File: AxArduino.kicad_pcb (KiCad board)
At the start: 2 copper layers, 86 x 33 mm, 35 parts, among them P1 CONN_01X02, P10 CONN_01X04, P11 CONN_01X04, P2 CONN_01X02, P3 CONN_01X03, P4 CONN_01X03, P5 CONN_01X03, P7 CONN_01X03, P8 CONN_01X15, P9 CONN_01X15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

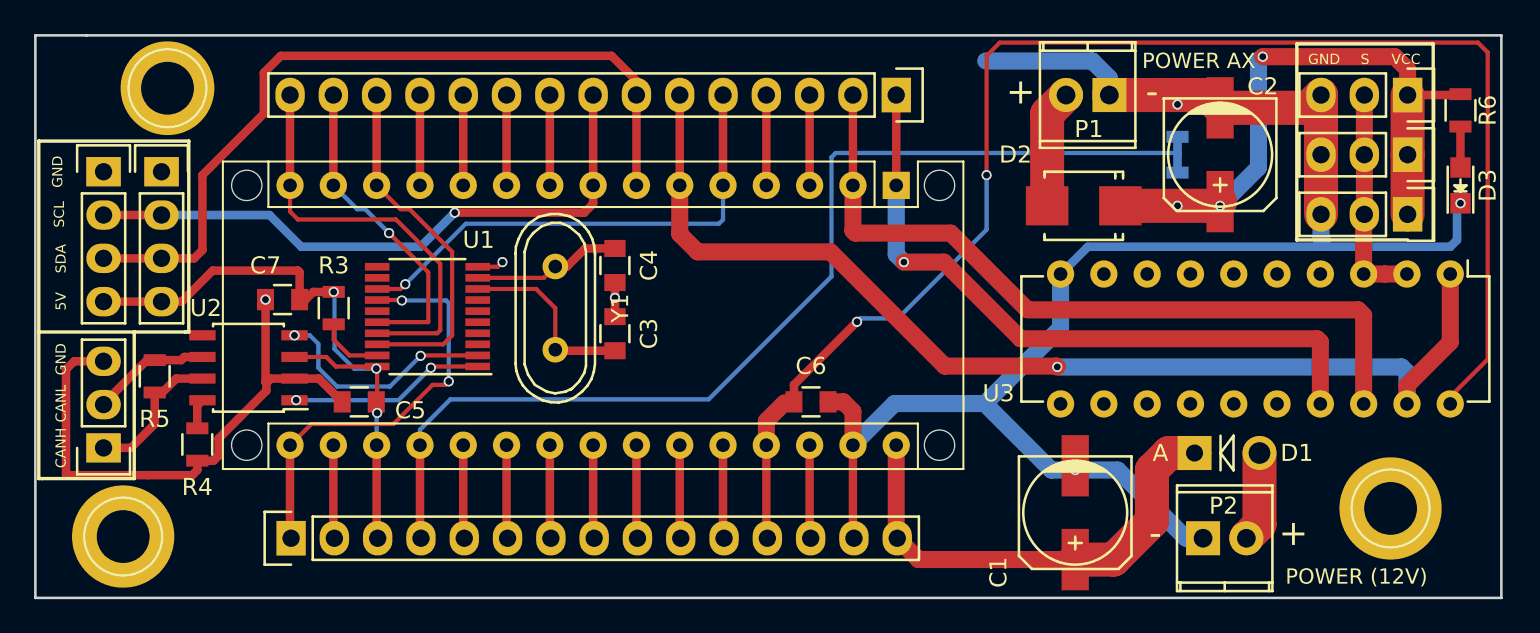
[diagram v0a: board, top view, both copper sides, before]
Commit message: Fixed stuff, like moving r to top layer and adding pullups to i2c
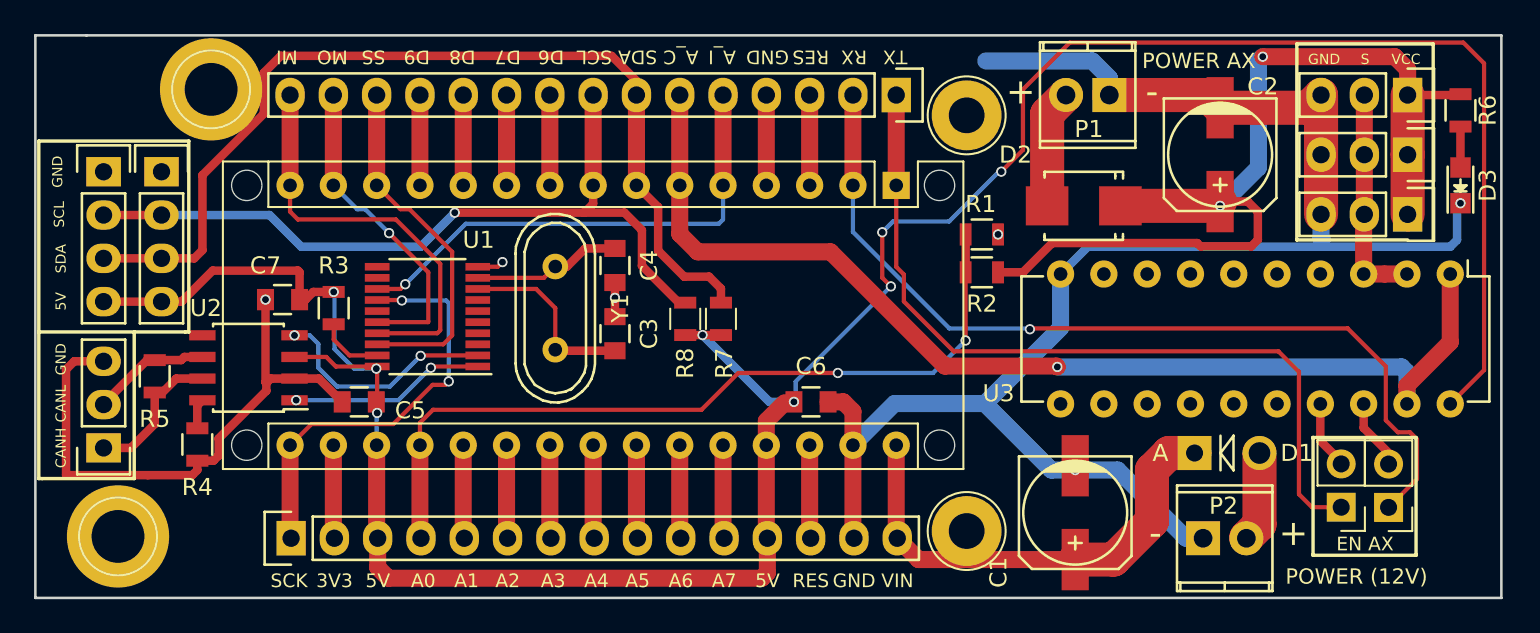
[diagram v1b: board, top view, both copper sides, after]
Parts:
- removed the G*** at (70.0, 87.2)
- removed the REF** at (56.8, 74.1)
- removed the REF** at (54.1, 100.4)
- removed the REF** at (128.5, 98.8)
- added G***: LOGO, Hardware:EP_Logo, B.Cu at (118.2, 77.9)
- added JP1: Jumper, Pin_Headers:Pin_Header_Straight_1x02_Pitch2.54mm, F.Cu at (128.4, 98.7)
- added JP2: Jumper, Pin_Headers:Pin_Header_Straight_1x02_Pitch2.54mm, F.Cu at (125.6, 98.7)
- added R7: 4K7, Resistors_SMD:R_0805, F.Cu at (89.2, 87.6)
- added R8: 4K7, Resistors_SMD:R_0805, F.Cu at (87.1, 87.6)
- added REF**: 1pin, Connectors:1pin, F.Cu at (53.8, 100.4)
- added REF**: 1pin, Connectors:1pin, F.Cu at (59.3, 74.2)
- added REF**: 1pin, Connectors:1pin, F.Cu at (103.6, 75.7)
- added REF**: 1pin, Connectors:1pin, F.Cu at (103.6, 100.1)
- R1, R2: moved to F.Cu
- moved R2 13.3 mm to (104.5, 82.7), turned to 0 degrees
- moved R1 12.5 mm to (104.5, 84.9), turned to 180 degrees
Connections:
- U1 pad 11: (no net) -> Net-(U1-Pad11)
- U1 pad 12: (no net) -> Net-(U1-Pad12)
- U1 pad 15: (no net) -> Net-(U1-Pad15)
- U1 pad 3: (no net) -> Net-(U1-Pad3)
- U1 pad 4: (no net) -> Net-(U1-Pad4)
- U1 pad 5: (no net) -> Net-(U1-Pad5)
- U1 pad 6: (no net) -> Net-(U1-Pad6)
- U1 pad 7: (no net) -> Net-(U1-Pad7)
- U2 pad 5: (no net) -> Net-(U2-Pad5)
- U3 pad 11: (no net) -> Net-(U3-Pad11)
- U3 pad 12: (no net) -> Net-(U3-Pad12)
- U3 pad 13: (no net) -> Net-(U3-Pad13)
- U3 pad 14: (no net) -> Net-(U3-Pad14)
- U3 pad 15: (no net) -> Net-(U3-Pad15)
- U3 pad 16: (no net) -> Net-(U3-Pad16)
- U3 pad 17: A_TX -> A_LS_TX
- U3 pad 18: A_RX -> A_LS_RX
- U3 pad 4: (no net) -> Net-(U3-Pad4)
- U3 pad 5: (no net) -> Net-(U3-Pad5)
- U3 pad 6: (no net) -> Net-(U3-Pad6)
- U3 pad 7: (no net) -> Net-(U3-Pad7)
- U3 pad 8: (no net) -> Net-(U3-Pad8)
- U3 pad 9: (no net) -> Net-(U3-Pad9)
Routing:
- net +5V: track 134.7 -> 164.2 mm, vias 5 -> 8
- net AX_P: track 42.4 -> 62.7 mm, vias 3 -> 2
- net A_A0: track 63.8 -> 47.1 mm, vias 0 -> 2
- net A_SDA: track 46.9 -> 56.7 mm
- net A_SCL: track 36.9 -> 46.3 mm
- net A_RX: track 45.2 -> 52.7 mm, vias 0 -> 1
- net A_TX: track 40.0 -> 47.2 mm, vias 1 -> 0
- net A_LS_RX: track 0.00 -> 4.29 mm
- net A_LS_TX: track 0.00 -> 4.03 mm
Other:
- board text added: "3V3"
- board text added: "A0"
- board text added: "A1"
- board text added: "A2"
- board text added: "A3"
- board text added: "A4"
- board text added: "A5"
- board text added: "A6"
- board text added: "A7"
- board text added: "A_C"
- board text added: "A_I"
- board text added: "D6"
- board text added: "D7"
- board text added: "D8"
- board text added: "D9"
- board text added: "EN AX"
- board text added: "MI"
- board text added: "MO"
- board text added: "RES"
- board text added: "RX"
- board text added: "SCK"
- board text added: "SS"
- board text added: "TX"
- board text added: "VIN"

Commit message: New design
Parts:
- removed C4: C, Capacitors_SMD:C_0805
- removed the G*** at (118.2, 77.9)
- removed P10: CONN_01X04, Pin_Headers:Pin_Header_Straight_1x04
- removed R3: 10K, Resistors_SMD:R_0805
- removed R4: 4.7K, Resistors_SMD:R_0805
- removed R5: 120, Resistors_SMD:R_0805
- removed the REF** at (53.8, 100.4)
- removed the REF** at (59.3, 74.2)
- removed the REF** at (103.6, 75.7)
- removed the REF** at (103.6, 100.1)
- removed U1: MCP2515-I/ST, Housings_SSOP:TSSOP-20_4.4x6.5mm_Pitch0.65mm
- removed U2: MCP2551-I-SN, Housings_SOIC:SOIC-8_3.9x4.9mm_Pitch1.27mm
- removed Y1: Crystal, Crystals:Crystal_HC49-U_Vertical
- added G***: LOGO, Hardware:EP_Logo, B.Cu at (92.7, 103.4)
- added G***: LOGO, Hardware:EP_Logo, F.Cu at (123.4, 111.5)
- added P12: CONN_01X03, Pin_Headers:Pin_Header_Straight_1x03_Pitch2.54mm, F.Cu at (88.5, 110.6)
- added P6: CONN_01X02, Connectors_Terminal_Blocks:TerminalBlock_Pheonix_MKDS1.5-2pol, F.Cu at (95.2, 96.0)
- added REF**: 1pin, Connectors:1pin, F.Cu at (171.7, 122.9)
- added REF**: 1pin, Connectors:1pin, F.Cu at (172.7, 93.9)
- added REF**: 1pin, Connectors:1pin, F.Cu at (132.2, 94.1)
- added REF**: 1pin, Connectors:1pin, F.Cu at (101.2, 94.1)
- added REF**: 1pin, Connectors:1pin, F.Cu at (98.8, 123.3)
- added REF***: ESD-Logo_6.6x6mm_SilkScreen, Symbols:ESD-Logo_6.6x6mm_SilkScreen, F.Cu at (114.6, 94.2)
- added REF***: OSHW-Logo_5.7x6mm_SilkScreen, Symbols:OSHW-Logo_5.7x6mm_SilkScreen, F.Cu at (108.0, 94.2)
- added REF***: KiCad-Logo2_6mm_SilkScreen, Symbols:KiCad-Logo2_6mm_SilkScreen, B.Cu at (162.8, 94.5)
- C1, C2: footprint Capacitors_SMD:c_elec_6.3x5.3 -> Capacitors_SMD:CP_Elec_6.3x5.3
- C3: value C -> CP; footprint Capacitors_SMD:C_0805 -> Capacitors_SMD:CP_Elec_6.3x5.3
- P1, P2: footprint Terminal_Blocks:TerminalBlock_Pheonix_MPT-2.54mm_2pol -> Connectors_Terminal_Blocks:TerminalBlock_Pheonix_MKDS1.5-2pol
- P11: footprint Pin_Headers:Pin_Header_Straight_1x04 -> Pin_Headers:Pin_Header_Straight_1x04_Pitch2.54mm
- P3, P4, P5, P7: footprint Pin_Headers:Pin_Header_Straight_1x03 -> Pin_Headers:Pin_Header_Straight_1x03_Pitch2.54mm
- P8, P9: footprint Pin_Headers:Pin_Header_Straight_1x15 -> Pin_Headers:Pin_Header_Straight_1x15_Pitch2.54mm
- moved C6 82.6 mm to (173.5, 116.6)
- moved C5 70.9 mm to (135.1, 115.3), turned to 0 degrees
- moved P11 65.6 mm to (119.8, 95.6), turned to 90 degrees
- moved P5 61.2 mm to (88.5, 119.9), turned to 90 degrees
- moved R1 60.8 mm to (162.3, 103.8)
- moved R2 56.6 mm to (157.1, 103.8), turned to 180 degrees
- moved C7 53.6 mm to (108.7, 115.3)
- moved R6 52.6 mm to (174.5, 107.2)
- moved D3 52.2 mm to (174.5, 111.0)
- moved P8 47.5 mm to (140.2, 99.1)
- moved C2 47.3 mm to (161.7, 97.2), turned to 90 degrees
- moved A1 46.9 mm to (140.2, 103.1)
- moved P9 46.2 mm to (104.6, 122.4)
- moved P1 46.1 mm to (152.9, 95.8)
- moved D1 44.8 mm to (152.7, 122.7), turned to 90 degrees
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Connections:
- A1 pad 11: A_D8 -> A_CONTROL
- A1 pad 6: A_CONTROL -> A_D3
- C3 pad 1: Net-(C3-Pad1) -> A_A1
- P5 pad 1: AX_P -> GND
- P5 pad 2: AX_S -> A_MOSI
- P5 pad 3: GND -> A_SS
- P7 pad 1: Net-(P7-Pad1) -> A_A1
- P7 pad 2: Net-(P7-Pad2) -> A_D6
- P8 pad 11: A_D8 -> A_CONTROL
- P8 pad 6: A_CONTROL -> A_D3
- U3 pad 11: Net-(U3-Pad11) -> (no net)
- U3 pad 12: Net-(U3-Pad12) -> (no net)
- U3 pad 13: Net-(U3-Pad13) -> (no net)
- U3 pad 14: Net-(U3-Pad14) -> (no net)
- U3 pad 15: Net-(U3-Pad15) -> (no net)
- U3 pad 16: Net-(U3-Pad16) -> (no net)
- U3 pad 4: Net-(U3-Pad4) -> (no net)
- U3 pad 5: Net-(U3-Pad5) -> (no net)
- U3 pad 6: Net-(U3-Pad6) -> (no net)
- U3 pad 7: Net-(U3-Pad7) -> (no net)
- U3 pad 8: Net-(U3-Pad8) -> (no net)
- U3 pad 9: Net-(U3-Pad9) -> (no net)
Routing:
- net A_A1: track 5.57 -> 53.4 mm
- net A_SDA: track 56.7 -> 10.1 mm
- net A_RX: track 52.7 -> 13.1 mm, vias 1 -> 0
- net A_TX: track 47.2 -> 8.20 mm
- net A_LS_RX: track 4.29 -> 41.6 mm, vias 0 -> 1
- net A_SCL: track 46.3 -> 10.5 mm, vias 1 -> 0
- net A_D6: track 5.30 -> 40.7 mm, vias 0 -> 2
- net A_LS_TX: track 4.03 -> 37.9 mm, vias 0 -> 1
- net A_D9: track 5.30 -> 30.8 mm
- net A_INT: track 29.3 -> 4.06 mm, vias 1 -> 0
- net AX_P: track 62.7 -> 38.9 mm, vias 2 -> 1
- net GND: track 148.7 -> 172.1 mm, vias 6 -> 3
- net A_SCK: track 25.3 -> 4.06 mm, vias 2 -> 0
- net A_MISO: track 24.6 -> 4.06 mm
- net A_A0: track 47.1 -> 63.8 mm
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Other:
- board size 86 x 33 mm -> 90.2 x 36.2 mm
- board text added: "2x PWM Servo"
- board text added: "5V Input"
- board text added: "6"
- board text added: "9"
- board text added: "AX-12"
- board text added: "AX-Arduino V1.1 https://github.com/Elektropioneer http://elektropioneer.co.rs"
- board text removed: "+"
- board text removed: "-"
- board text removed: "3V3"
- board text removed: "A0"
- board text removed: "A1"
- board text removed: "A2"
- board text removed: "A3"
- board text removed: "A4"
- board text removed: "A5"
- board text removed: "A6"
- board text removed: "A7"
- board text removed: "AX-12 driver 74LS241"
- board text removed: "A_C"
- board text removed: "A_I"
- board text removed: "CAN"
- board text removed: "CANH"
- board text removed: "CANL"
- board text removed: "D6"
- board text removed: "D7"
- board text removed: "D8"
- board text removed: "D9"
- board text removed: "I2C"
- board text removed: "MI"
- board text removed: "MO"
- board text removed: "POWER (12V)"
- board text removed: "POWER AX"
- board text removed: "RES"
- board text removed: "SCK"
- board text removed: "SS"
- board text removed: "VIN"
- board text removed: "http://elektropioneer.co.rs/ https://github.com/Elektropioneer Arduino_CAN_AX"

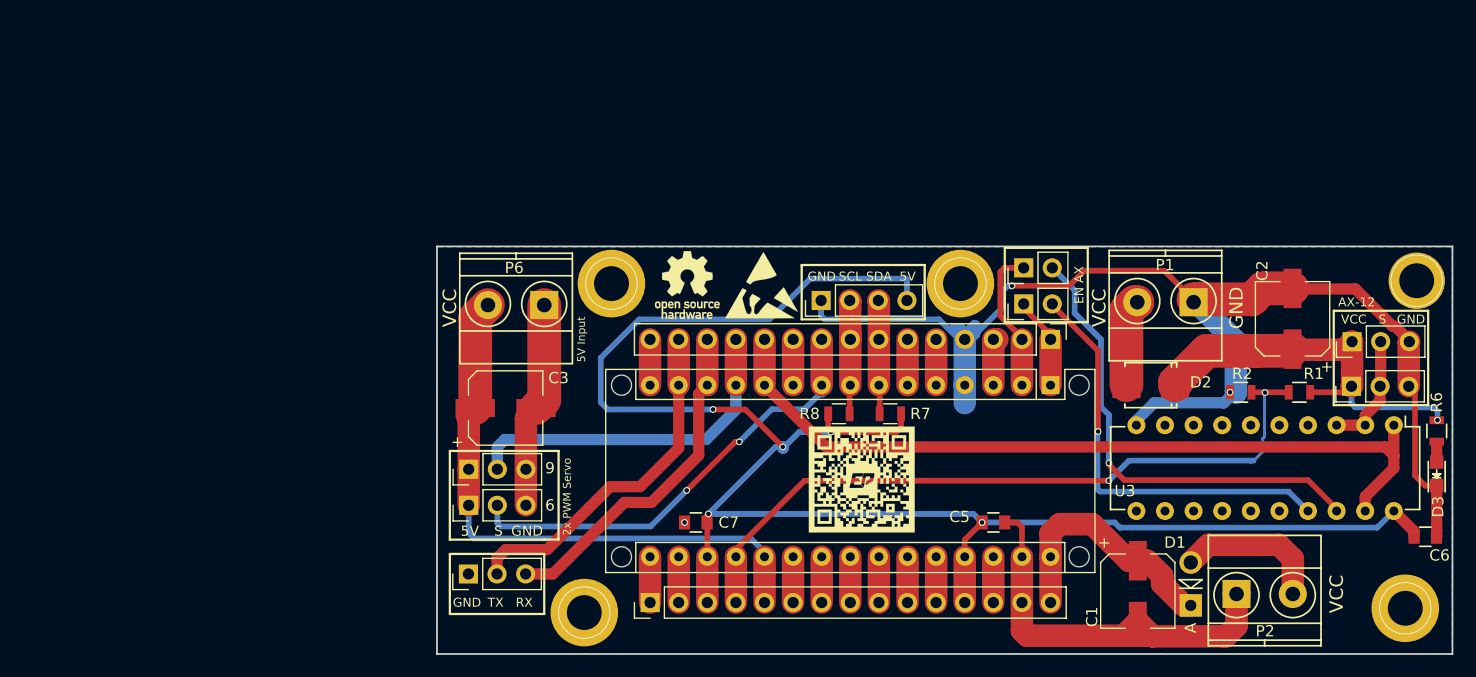
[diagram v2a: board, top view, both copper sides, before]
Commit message: Small modifs, added connectors and servo support
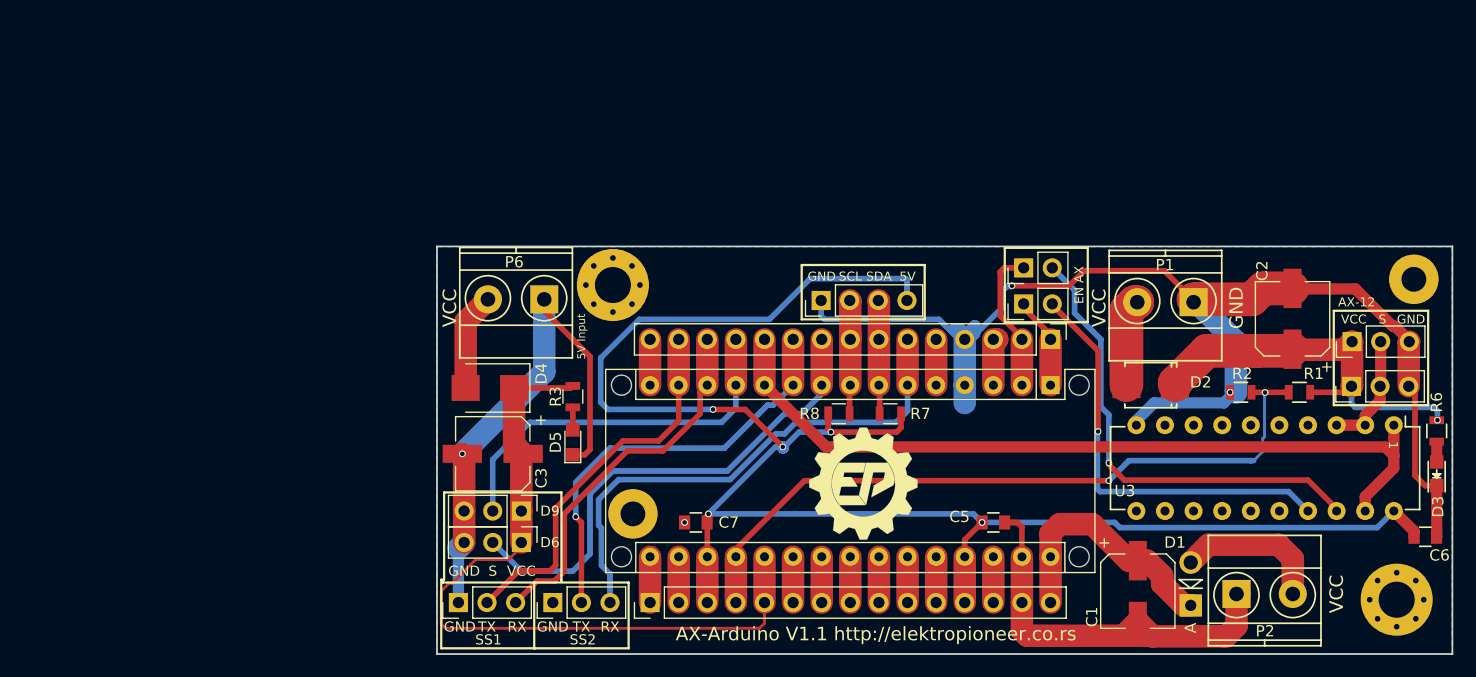
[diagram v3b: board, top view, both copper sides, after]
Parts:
- removed the G*** at (92.7, 103.4)
- removed the G*** at (123.4, 111.5)
- removed REF** (x5): 1pin, Connectors:1pin
- removed REF***: ESD-Logo_6.6x6mm_SilkScreen, Symbols:ESD-Logo_6.6x6mm_SilkScreen
- removed REF***: OSHW-Logo_5.7x6mm_SilkScreen, Symbols:OSHW-Logo_5.7x6mm_SilkScreen
- removed REF***: KiCad-Logo2_6mm_SilkScreen, Symbols:KiCad-Logo2_6mm_SilkScreen
- added D4: D_Schottky, Diodes_SMD:D_SMB_Standard, F.Cu at (90.4, 103.4)
- added D5: LED, LEDs:LED_0805, F.Cu at (97.8, 108.2)
- added G***: LOGO, Hardware:EP_Logo_3, B.Cu at (159.9, 98.4)
- added G***: LOGO, Hardware:github_logo, B.Cu at (93.4, 104.7)
- added G***: LOGO, Hardware:EP_Logo_3, F.Cu at (123.7, 111.5)
- added MK1: Mounting_Hole, Mounting_Holes:MountingHole_3.2mm_M3_Pad_Via, F.Cu at (170.9, 122.2)
- added MK2: Mounting_Hole, Mounting_Holes:MountingHole_3.2mm_M3_Pad_Via, F.Cu at (101.3, 94.2)
- added MK3: Mounting_Hole, Mounting_Holes:MountingHole_2.2mm_M2_Pad, F.Cu at (103.1, 114.6)
- added MK4: Mounting_Hole, Mounting_Holes:MountingHole_2.2mm_M2_Pad, F.Cu at (172.5, 93.7)
- added P10: CONN_01X03, Pin_Headers:Pin_Header_Straight_1x03_Pitch2.54mm, F.Cu at (96.0, 122.4)
- added R3: R, Resistors_SMD:R_0805, F.Cu at (97.8, 104.1)
- moved P12 5.97 mm to (93.2, 114.3), turned to 270 degrees
- moved P7 5.72 mm to (93.2, 117.1), turned to 270 degrees
- moved C3 4.22 mm to (90.7, 109.2), turned to 180 degrees
- moved P5 2.69 mm to (87.6, 122.4)
- moved P6 0.51 mm to (95.2, 95.5)
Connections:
- P6 pad 2: A_A1 -> Net-(D4-Pad2)
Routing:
- net A_D3: track 4.06 -> 46.6 mm
- net A_D7: track 4.06 -> 37.8 mm, vias 0 -> 1
- net GND: track 172.1 -> 201.4 mm, vias 3 -> 4
- net A_A1: track 53.4 -> 66.8 mm
- net Net-(D4-Pad2): track 0.00 -> 8.69 mm
- net A_D6: track 40.7 -> 45.3 mm, vias 2 -> 0
- net A_D9: track 30.8 -> 34.2 mm
- net A_MOSI: track 31.7 -> 34.7 mm
- net A_SS: track 30.5 -> 33.3 mm
- net Net-(D5-Pad2): track 0.00 -> 2.01 mm
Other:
- board text added: "1"
- board text added: "AX-Arduino V1.1 http://elektropioneer.co.rs"
- board text added: "D6"
- board text added: "D9"
- board text added: "SS1"
- board text added: "SS2"
- board text removed: "2x PWM Servo"
- board text removed: "6"
- board text removed: "9"
